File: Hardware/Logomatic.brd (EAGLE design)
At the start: 61 x 38.1 mm, 63 parts, among them Q1 12MHz, Q2 32kHz, Q4 TRANSISTOR_PNPSMD, U1 MCP73831, U2 3.3V, U3 USD-SOCKETNEW, U4 LPC213X, X1 USBSMD

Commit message: Version 2.7 board commit
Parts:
- removed U$9: CREATIVE_COMMONS, SparkFun:CREATIVE_COMMONS
- added FRAME2, FRAME4: FRAME-LETTER, SparkFun-Aesthetics:CREATIVE_COMMONS
- added LOGO1: OSHW-LOGOL, SparkFun-Aesthetics:OSHW-LOGO-L
- added LOGO2: SFE_LOGO_NAME.1_INCH, SparkFun-Aesthetics:SFE_LOGO_NAME_.1
- added U$10: REVISION, SparkFun-Aesthetics:REVISION
- C1, C10, C11, C12, C13, C14, C15, C16, C2, C3, C4, C7, C8, C9: device SparkFunEagle-6-6-07:C0402 -> SparkFun-Capacitors:0603-CAP
- C17, C5: device SparkFun:0402-CAP -> SparkFun-Capacitors:0603-CAP
- C6: device SparkFun:EIA3216 -> SparkFun-Capacitors:EIA3216
- R1, R12, R13, R14, R15, R4, R5, R6, R7, R8: device SparkFunEagle-6-6-07:C0402 -> SparkFun-Resistors:0603-RES
- R10, R11, R9: device SparkFunEagle-6-6-07:C0402 -> SparkFun-Resistors:0603
- R16, R17, R2, R3: device SparkFun:0402-RES -> SparkFun-Resistors:0603-RES
- U$6: value LOGO-SFENEW -> SFE_LOGO_FLAME1_INCH; device SparkFun:SFE-NEW-WEBLOGO -> SparkFun-Aesthetics:SFE_LOGO_FLAME_.9
- U3: device SparkFun:MICRO-SD-SOCKET-PP -> SparkFun-Connectors:MICRO-SD-SOCKET-PP
- X1: value USBSMD -> USB_MICROB_PLUGCONN-11752; device SparkFun:USB-MINIB -> SparkFun-Connectors:USB-B-MICRO-SMD_V03
- moved U$6 50.4 mm to (12.2, 12.2), turned to 90 degrees
- moved U$7 35.2 mm to (6.86, 33.7)
- moved C7 6.48 mm to (21.6, 31.8), turned to 180 degrees
- moved C2 4.45 mm to (55.2, 6.35)
- moved R12 4.02 mm to (49.5, 6.35), turned to 90 degrees
- moved R14 3.81 mm to (53.3, 6.35)
- moved X1 3.81 mm to (59.7, 11.3)
- moved C13 3.59 mm to (17.8, 16.5), turned to 0 degrees
- moved R8 3.18 mm to (51.4, 6.35)
- moved C3 3.17 mm to (52.7, 15.2), turned to 180 degrees
- moved C4 3.17 mm to (52.7, 10.2)
- moved R10 3.17 mm to (52.7, 11.4)
- moved R9 3.17 mm to (52.7, 14.0), turned to 180 degrees
- moved C12 2.84 mm to (17.8, 14.0), turned to 0 degrees
- moved C8 2.54 mm to (26.7, 11.4)
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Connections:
- net GND: now also X1.GND1; no longer X1.GND
- net USB_D+: now also X1.D+1; no longer X1.D+
- net USB_D-: now also X1.D-1; no longer X1.D-
- net USB_VIN: now also X1.VBUS1; no longer X1.VBUS
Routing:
- net N$16: track 34.6 -> 40.4 mm
- net N$31: track 18.9 -> 24.2 mm
- net P-D+: track 26.4 -> 31.2 mm
- net N$17: track 3.50 -> 7.37 mm
- net USB_D+: track 5.43 -> 9.12 mm
- net P-D-: track 26.6 -> 29.3 mm
- net RAW: track 54.6 -> 52.0 mm
- net N$13: track 1.33 -> 3.85 mm
- net N$12: track 3.42 -> 5.66 mm
- net BATTLVL: track 24.9 -> 26.9 mm
- net N$5: track 8.93 -> 7.14 mm
- net STAT1: track 16.2 -> 17.7 mm
- net STAT: track 4.85 -> 3.39 mm
- net RST: track 40.0 -> 41.4 mm
- net VCC: track 174.5 -> 173.5 mm
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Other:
- board text added: "Logomatic"
- board text added: "Toni Klopfenstein"
- board text added: "v27"
- board text removed: "10-10-10"
- board text removed: "Logomatic v2"
- board text removed: "SparkFun Electronics"

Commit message: Updating to fancy new silk on board
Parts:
- added LOGO3: SFE_LOGO_FLAME.4_INCH, SparkFun-Aesthetics:SFE_LOGO_FLAME_.4
- U$6: value SFE_LOGO_FLAME1_INCH -> LOGOMATIC_LOGO; device SparkFun-Aesthetics:SFE_LOGO_FLAME_.9 -> SparkFun-Aesthetics:LOGOMATIC_LOGO
- moved U$6 32.7 mm to (44.5, 17.8), turned to 0 degrees
- moved LOGO1 30.9 mm to (17.8, 10.2), turned to 0 degrees
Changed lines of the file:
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@@
 <setting verticaltext="up"/>
 </settings>
-<grid distance="0.025" unitdist="inch" unit="inch" style="lines" multiple="1" display="yes" altdistance="0.005" altunitdist="inch" altunit="inch"/>
+<grid distance="0.05" unitdist="inch" unit="inch" style="lines" multiple="1" display="yes" altdistance="0.005" altunitdist="inch" altunit="inch"/>
 <layers>
 <layer number="1" name="Top" color="4" fill="1" visible="yes" active="yes"/>
@@
 <layer number="47" name="Measures" color="7" fill="1" visible="no" active="yes"/>
 <layer number="48" name="Document" color="7" fill="1" visible="no" active="yes"/>
-<layer number="49" name="Reference" color="7" fill="1" visible="yes" active="yes"/>
+<layer number="49" name="Reference" color="7" fill="1" visible="no" active="yes"/>
 <layer number="50" name="dxf" color="7" fill="1" visible="no" active="yes"/>
 <layer number="51" name="tDocu" color="6" fill="1" visible="yes" active="yes"/>
@@
 <attribute name="VALUE" value="0.1uF" x="17.78" y="13.97" size="1.778" layer="27" display="off"/>
 </element>
-<element name="U$6" library="SparkFun-Aesthetics" package="SFE_LOGO_FLAME_.9" value="SFE_LOGO_FLAME1_INCH" x="12.192" y="12.192" rot="MR90"/>
 <element name="R16" library="SparkFun-Resistors" package="0603-RES" value="1M" x="12.7" y="18.415">
 <attribute name="PROD_ID" value="RES-07868" x="12.7" y="18.415" size="1.778" layer="27" display="off"/>
@@
 <element name="FRAME4" library="SparkFun-Aesthetics" package="CREATIVE_COMMONS" value="FRAME-LETTER" x="9.18104375" y="-10.16"/>
 <element name="U$10" library="SparkFun-Aesthetics" package="REVISION" value="REVISION" x="20.828" y="-12.827"/>
-<element name="LOGO1" library="SparkFun-Aesthetics" package="OSHW-LOGO-L" value="OSHW-LOGOL" x="46.99" y="20.32" rot="MR90"/>
+<element name="LOGO1" library="SparkFun-Aesthetics" package="OSHW-LOGO-L" value="OSHW-LOGOL" x="17.78" y="10.16" rot="MR0"/>
 <element name="LOGO2" library="SparkFun-Aesthetics" package="SFE_LOGO_NAME_.1" value="SFE_LOGO_NAME.1_INCH" x="0" y="29.845"/>
+<element name="U$6" library="SparkFun-Aesthetics" package="LOGOMATIC_LOGO" value="LOGOMATIC_LOGO" x="44.45" y="17.78" rot="MR0"/>
+<element name="LOGO3" library="SparkFun-Aesthetics" package="SFE_LOGO_FLAME_.4" value="SFE_LOGO_FLAME.4_INCH" x="46.99" y="5.08" rot="MR0"/>
 </elements>
 <signals>

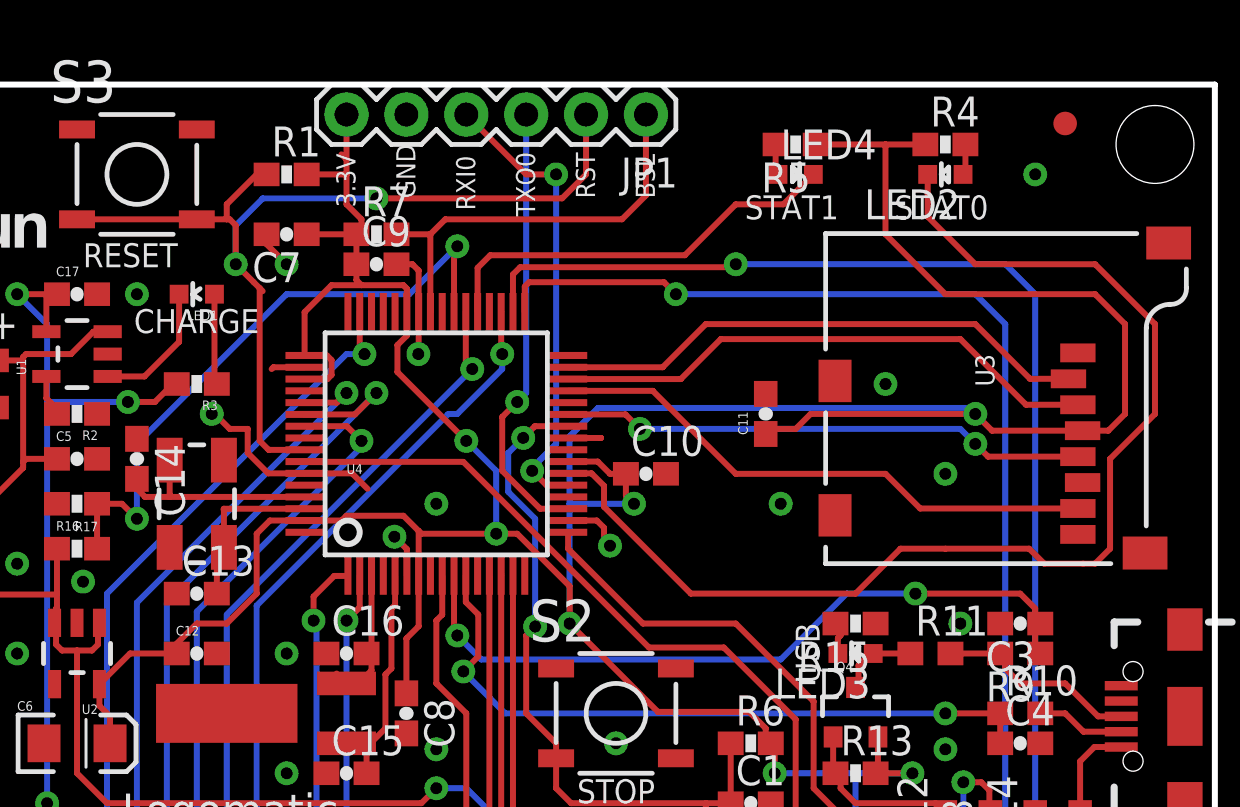
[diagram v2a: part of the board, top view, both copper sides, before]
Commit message: Changing 0603 LED package
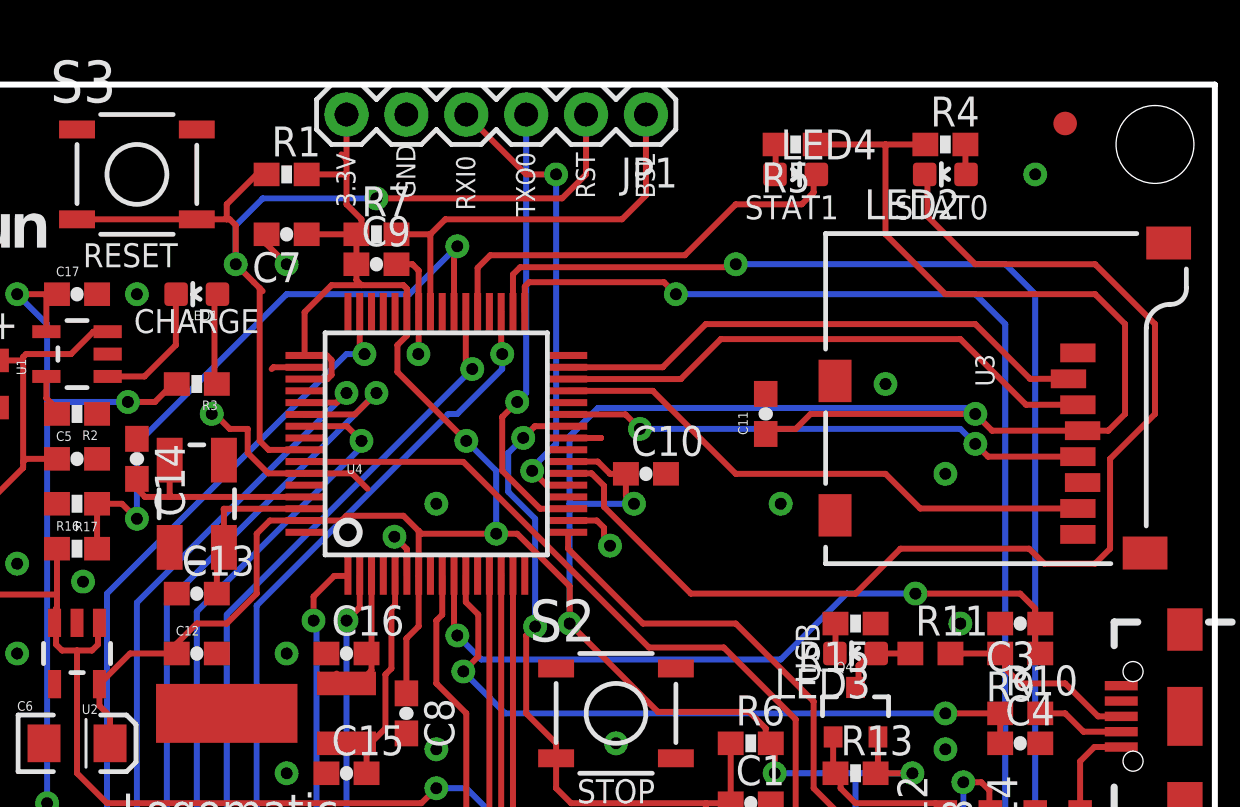
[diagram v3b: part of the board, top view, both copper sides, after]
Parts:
- LED1: device SparkFun:LED-0603 -> SparkFun-LED:LED-0603
- LED2, LED4: device SparkFunEagle-6-6-07:LED-0603 -> SparkFun-LED:LED-0603
- LED3: device SparkFun_Master:LED-0603 -> SparkFun-LED:LED-0603
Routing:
- net STAT1: track 17.7 -> 18.3 mm
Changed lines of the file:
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@@
 <elements>
 <element name="U4" library="SparkFun" package="SQFP-S-10X10-64" value="LPC213X" x="27.94" y="22.86"/>
-<element name="LED3" library="SparkFun_Master" package="LED-0603" value="" x="45.72" y="13.97" smashed="yes" rot="R90">
+<element name="LED3" library="SparkFun-LED" package="LED-0603" value="" x="45.72" y="13.97" smashed="yes" rot="R90">
 <attribute name="NAME" x="46.355" y="13.335" size="1.27" layer="25" rot="R180"/>
-<attribute name="VALUE" x="46.355" y="15.875" size="1.27" layer="27" rot="R180"/>
+<attribute name="VALUE" value="RED" x="46.355" y="15.875" size="1.27" layer="27" rot="R180"/>
+<attribute name="PROD_ID" value="DIO-00819" x="45.72" y="13.97" size="1.778" layer="27" rot="R90" display="off"/>
 </element>
 <element name="X1" library="SparkFun-Connectors" package="USB-B-MICRO-SMD_V03" value="USB_MICROB_PLUGCONN-11752" x="59.69" y="11.303" rot="R180">
@@
 <element name="S2" library="SparkFunEagle-6-6-07" package="TACTILE_SWITCH_SMD" value="Stop" x="35.56" y="11.43"/>
 <element name="S3" library="SparkFunEagle-6-6-07" package="TACTILE_SWITCH_SMD" value="Reset" x="15.24" y="34.29"/>
-<element name="LED2" library="SparkFunEagle-6-6-07" package="LED-0603" value="RED" x="49.53" y="34.29" smashed="yes" rot="R90">
+<element name="LED2" library="SparkFun-LED" package="LED-0603" value="RED" x="49.53" y="34.29" smashed="yes" rot="R90">
 <attribute name="NAME" x="50.165" y="33.655" size="1.27" layer="25" rot="R180"/>
-<attribute name="VALUE" x="50.8508" y="36.068" size="0.6096" layer="27" rot="R270"/>
-</element>
-<element name="LED4" library="SparkFunEagle-6-6-07" package="LED-0603" value="GREEN" x="43.18" y="34.29" smashed="yes" rot="R270">
+<attribute name="VALUE" value="RED" x="50.8508" y="36.068" size="0.6096" layer="27" rot="R270"/>
+<attribute name="PROD_ID" value="DIO-00819" x="49.53" y="34.29" size="1.778" layer="27" rot="R90" display="off"/>
+</element>
+<element name="LED4" library="SparkFun-LED" package="LED-0603" value="GREEN" x="43.18" y="34.29" smashed="yes" rot="R270">
 <attribute name="NAME" x="42.545" y="34.925" size="1.27" layer="25"/>
-<attribute name="VALUE" x="41.8592" y="31.9532" size="0.6096" layer="27" rot="R90"/>
+<attribute name="VALUE" value="GREEN" x="41.8592" y="31.9532" size="0.6096" layer="27" rot="R90"/>
+<attribute name="PROD_ID" value="DIO-00821" x="43.18" y="34.29" size="1.778" layer="27" rot="R270" display="off"/>
 </element>
 <element name="Q1" library="SparkFunEagle-6-6-07" package="CRYSTAL-SMD-5X3" value="12MHz" x="17.78" y="20.32" smashed="yes" rot="R270"/>
@@
 <attribute name="PROD_ID" value="CAP-08280" x="12.7" y="22.225" size="1.778" layer="27" display="off"/>
 </element>
-<element name="LED1" library="SparkFun" package="LED-0603" value="LED RED" x="17.78" y="29.21" smashed="yes" rot="R90">
+<element name="LED1" library="SparkFun-LED" package="LED-0603" value="LED RED" x="17.78" y="29.21" smashed="yes" rot="R90">
 <attribute name="NAME" x="18.669" y="28.5115" size="0.4064" layer="25" rot="R180"/>
-<attribute name="VALUE" x="18.8468" y="28.6639" size="0.4064" layer="27" rot="R180"/>
+<attribute name="VALUE" value="RED" x="18.8468" y="28.6639" size="0.4064" layer="27" rot="R180"/>
+<attribute name="PROD_ID" value="DIO-00819" x="17.78" y="29.21" size="1.778" layer="27" rot="R90" display="off"/>
 </element>
 <element name="U$1" library="SparkFun" package="FIDUCIAL-1X2" value="FIDUCIAL1X2" x="2.54" y="6.35"/>
@@
 <contactref element="LED3" pad="C"/>
 <contactref element="R15" pad="2"/>
-<wire x1="44.97" y1="13.97" x2="44.97" y2="14.617" width="0.254" layer="1"/>
-<wire x1="44.97" y1="14.617" x2="45.085" y2="14.732" width="0.254" layer="1"/>
-<wire x1="45.085" y1="15.24" x2="44.87" y2="15.24" width="0.254" layer="1"/>
-<wire x1="45.085" y1="14.732" x2="45.085" y2="15.24" width="0.254" layer="1"/>
+<wire x1="44.87" y1="15.24" x2="44.87" y2="13.997" width="0.254" layer="1"/>
+<wire x1="44.87" y1="13.997" x2="44.843" y2="13.97" width="0.254" layer="1"/>
 </signal>
 <signal name="P4">
@@
 <wire x1="35.052" y1="20.193" x2="38.735" y2="16.51" width="0.254" layer="1"/>
 <wire x1="38.735" y1="16.51" x2="45.72" y2="16.51" width="0.254" layer="1"/>
-<wire x1="45.72" y1="16.51" x2="46.99" y2="17.78" width="0.254" layer="1"/>
+<wire x1="45.72" y1="16.51" x2="47.625" y2="18.415" width="0.254" layer="1"/>
 <wire x1="55.88" y1="17.78" x2="56.515" y2="18.415" width="0.254" layer="1"/>
 <wire x1="56.515" y1="18.415" x2="56.515" y2="22.225" width="0.254" layer="1"/>
@@
 <wire x1="58.42" y1="27.94" x2="55.88" y2="30.48" width="0.254" layer="1"/>
 <wire x1="55.88" y1="30.48" x2="50.8" y2="30.48" width="0.254" layer="1"/>
-<wire x1="48.78" y1="32.5" x2="48.78" y2="34.29" width="0.254" layer="1"/>
-<wire x1="50.8" y1="30.48" x2="48.78" y2="32.5" width="0.254" layer="1"/>
-<wire x1="46.99" y1="17.78" x2="47.625" y2="18.415" width="0.254" layer="1"/>
-<wire x1="47.625" y1="18.415" x2="49.53" y2="18.415" width="0.254" layer="1"/>
-<wire x1="49.53" y1="18.415" x2="53.086" y2="18.415" width="0.254" layer="1"/>
+<wire x1="47.625" y1="18.415" x2="53.086" y2="18.415" width="0.254" layer="1"/>
 <wire x1="53.086" y1="18.415" x2="53.721" y2="17.78" width="0.254" layer="1"/>
-<wire x1="55.372" y1="17.78" x2="55.88" y2="17.78" width="0.254" layer="1"/>
-<wire x1="53.721" y1="17.78" x2="55.372" y2="17.78" width="0.254" layer="1"/>
+<wire x1="53.721" y1="17.78" x2="55.88" y2="17.78" width="0.254" layer="1"/>
+<wire x1="50.8" y1="30.48" x2="48.768" y2="32.512" width="0.254" layer="1"/>
+<wire x1="48.768" y1="32.512" x2="48.768" y2="34.175" width="0.254" layer="1"/>
+<wire x1="48.768" y1="34.175" x2="48.653" y2="34.29" width="0.254" layer="1"/>
 </signal>
 <signal name="SCK0">
@@
 <wire x1="30.226" y1="30.861" x2="38.481" y2="30.861" width="0.254" layer="1"/>
 <wire x1="38.481" y1="30.861" x2="40.64" y2="33.02" width="0.254" layer="1"/>
-<wire x1="40.64" y1="33.02" x2="42.66" y2="33.02" width="0.254" layer="1"/>
-<wire x1="42.66" y1="33.02" x2="43.93" y2="34.29" width="0.254" layer="1"/>
+<wire x1="40.64" y1="33.02" x2="43.434" y2="33.02" width="0.254" layer="1"/>
+<wire x1="43.434" y1="33.02" x2="43.942" y2="33.528" width="0.254" layer="1"/>
+<wire x1="43.942" y1="33.528" x2="43.942" y2="34.175" width="0.254" layer="1"/>
+<wire x1="43.942" y1="34.175" x2="44.057" y2="34.29" width="0.254" layer="1"/>
 </signal>
 <signal name="P8">
@@
 <contactref element="LED2" pad="A"/>
 <contactref element="R4" pad="2"/>
-<wire x1="50.38" y1="35.56" x2="50.38" y2="34.39" width="0.254" layer="1"/>
-<wire x1="50.38" y1="34.39" x2="50.28" y2="34.29" width="0.254" layer="1"/>
+<wire x1="50.38" y1="35.56" x2="50.38" y2="34.317" width="0.254" layer="1"/>
+<wire x1="50.38" y1="34.317" x2="50.407" y2="34.29" width="0.254" layer="1"/>
 </signal>
 <signal name="N$19">
 <contactref element="LED4" pad="A"/>
 <contactref element="R5" pad="2"/>
-<wire x1="42.33" y1="35.56" x2="42.33" y2="34.39" width="0.254" layer="1"/>
-<wire x1="42.33" y1="34.39" x2="42.43" y2="34.29" width="0.254" layer="1"/>
+<wire x1="42.33" y1="35.56" x2="42.33" y2="34.317" width="0.254" layer="1"/>
+<wire x1="42.33" y1="34.317" x2="42.303" y2="34.29" width="0.254" layer="1"/>
 </signal>
 <signal name="N$5">
@@
 <contactref element="U1" pad="1"/>
 <wire x1="14.0001" y1="25.72" x2="15.56" y2="25.72" width="0.254" layer="1"/>
-<wire x1="17.03" y1="29.21" x2="17.03" y2="27.19" width="0.254" layer="1"/>
-<wire x1="17.03" y1="27.19" x2="15.56" y2="25.72" width="0.254" layer="1"/>
+<wire x1="15.56" y1="25.72" x2="16.891" y2="27.051" width="0.254" layer="1"/>
+<wire x1="16.891" y1="27.051" x2="16.891" y2="29.198" width="0.254" layer="1"/>
+<wire x1="16.891" y1="29.198" x2="16.903" y2="29.21" width="0.254" layer="1"/>
 </signal>
 <signal name="N$13">
 <contactref element="R3" pad="1"/>
 <contactref element="LED1" pad="A"/>
-<wire x1="18.53" y1="29.21" x2="18.53" y2="25.5" width="0.254" layer="1"/>
 <wire x1="18.53" y1="25.5" x2="18.63" y2="25.4" width="0.254" layer="1"/>
+<wire x1="18.53" y1="25.5" x2="18.53" y2="29.083" width="0.254" layer="1"/>
+<wire x1="18.53" y1="29.083" x2="18.657" y2="29.21" width="0.254" layer="1"/>
 </signal>
 <signal name="STAT">
@@
 <wire x1="45.72" y1="12.53" x2="45.72" y2="12.573" width="0.254" layer="1"/>
 <wire x1="45.72" y1="12.573" x2="45.847" y2="12.7" width="0.254" layer="1"/>
-<wire x1="46.355" y1="13.97" x2="46.47" y2="13.97" width="0.254" layer="1"/>
+<wire x1="46.355" y1="13.97" x2="46.597" y2="13.97" width="0.254" layer="1"/>
 <wire x1="45.847" y1="12.7" x2="45.847" y2="13.462" width="0.254" layer="1"/>
 <wire x1="45.847" y1="13.462" x2="46.355" y2="13.97" width="0.254" layer="1"/>
-<wire x1="48.045" y1="13.97" x2="46.47" y2="13.97" width="0.254" layer="1"/>
+<wire x1="48.045" y1="13.97" x2="46.597" y2="13.97" width="0.254" layer="1"/>
 </signal>
 <signal name="RAW">

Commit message: Sorted gitignore
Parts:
- added R18, R19, R20: 100k, SparkFun-Resistors:0603-RES
- J1: value USD-SOCKETNEW -> USD_CONNECTOR
- R1, R12, R13, R14, R16, R17, R6, R7, R8: device SparkFun-Resistors:0603-RES -> SparkFun-Resistors:0603-RES@1
- R10, R9: device SparkFun-Resistors:0603 -> SparkFun-Resistors:0603-RES
- R2: value 2K -> 2.0k
- renumbered U3 to J1
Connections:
- removed net CS0: J1.2, U4.31
- new net !CS0: J1.CS, U4.31
- new net CD: J1.CD2
- new net N$10: J1.RSV2, R19.1
- new net N$3: J1.CD1, R18.1
- new net N$4: J1.RSV1, R20.1
- net GND: now also J1.GND, J1.GND3; no longer J1.6, J1.CD2
- net MISO0: now also J1.DO; no longer J1.7
- net MOSI0: now also J1.DI; no longer J1.3
- net SCK0: now also J1.SCLK; no longer J1.5
- net VCC: now also J1.VCC, R18.2, R19.2, R20.2; no longer J1.4
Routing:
- net CS0: track 22.9 -> 0.00 mm
- net !CS0: track 0.00 -> 22.9 mm
